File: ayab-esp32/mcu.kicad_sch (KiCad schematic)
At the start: 27 parts, among them J201 SPARE1, J202 SPARE0, Q201 AO3400A, SW201 USER, SW202 RESET, SW203 BOOTSEL, U201 ESP32-S3-MINI-1

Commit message: Correct footprint and regenerate documentation
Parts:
- D204: LCSC ID C2290 -> C22452; OEM Hubei KENTO Elec -> (none)
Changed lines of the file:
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@@
       (effects (font (size 1.27 1.27)) hide)
     )
-    (property "LCSC ID" "C2290" (at 247.65 41.91 0)
+    (property "LCSC ID" "C22452" (at 247.65 41.91 0)
       (effects (font (size 1.27 1.27)) hide)
     )
-    (property "OEM" "Hubei KENTO Elec" (at 247.65 41.91 0)
+    (property "OEM" "" (at 247.65 41.91 0)
       (effects (font (size 1.27 1.27)) hide)
     )

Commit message: add mouser parts list
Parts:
- BUZZER201: Mouser PN (none) -> 179-CMT-8504-99SMTTR
- C201, C202, C203, C204: Mouser PN (none) -> 187-CL10B104MB8NNNC
- C205: Mouser PN (none) -> 963-TMK212BBJ106KG-T
- D201: Mouser PN (none) -> 755-SML-H12Y8TT86C
- D202: Mouser PN (none) -> 749-SM0805PGC
- D203: Mouser PN (none) -> 749-SM0805RC
- D204: Mouser PN (none) -> 750-SS54B-HF
- J201, J202: Mouser PN (none) -> 855-M20-9750446
- R201, R205, R206, R207, R208, R211: Mouser PN (none) -> 791-RMC16K103FTP
- R202, R203, R204: Mouser PN (none) -> 603-AC0603FR-135K1L
- R212: Mouser PN (none) -> 71-CRCW06030000Z0EC
- U201: Mouser PN (none) -> 356-ESP32-S3-MINI1N8

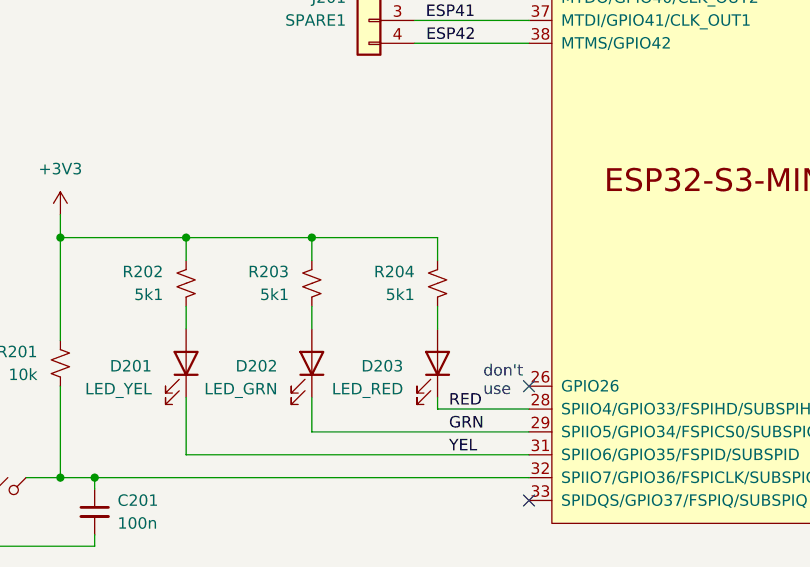
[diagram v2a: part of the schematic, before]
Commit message: address bringup issues
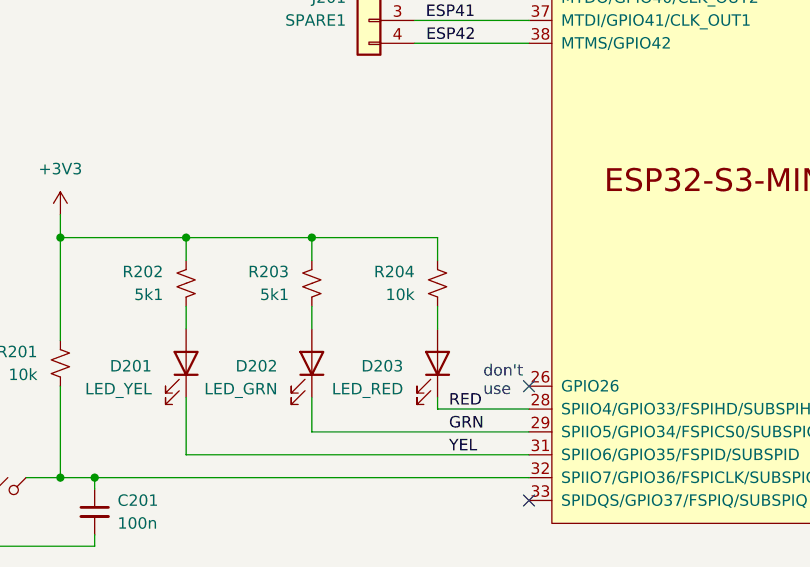
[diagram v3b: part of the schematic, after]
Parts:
- R204: value 5k1 -> 10k; LCSC ID C23186 -> C25804
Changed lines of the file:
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@@
 		(lib_id "ayab-lib:R_Small_US")
 		(at 83.82 104.14 0)
-		(mirror y)
 		(unit 1)
 		(exclude_from_sim no)
@@
 		(on_board yes)
 		(dnp no)
-		(fields_autoplaced yes)
 		(property "Reference" "R204"
-			(at 81.28 102.87 0)
+			(at 81.28 102.8699 0)
 			(effects
 				(font
 					(size 1.27 1.27)
 				)
-				(justify left)
+				(justify right)
 			)
 		)
-		(property "Value" "5k1"
-			(at 81.28 105.41 0)
+		(property "Value" "10k"
+			(at 81.28 105.4099 0)
 			(effects
 				(font
 					(size 1.27 1.27)
 				)
-				(justify left)
+				(justify right)
 			)
 		)
@@
 			)
 		)
-		(property "LCSC ID" "C23186"
+		(property "LCSC ID" "C25804"
 			(at 83.82 104.14 0)
 			(effects

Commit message: clean ERC DRC, fix library paths
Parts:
- BUZZER201: footprint easyeda2kicad:BUZ-SMD_4P-L8.5-W8.5-P8.50-BR -> Library:BUZ-SMD_4P-L8.5-W8.5-P8.50-BR
- SW201, SW202, SW203: footprint easyeda2kicad:KEY-TH_4P-L7.5-W11.5-P4.5 -> Library:KEY-TH_4P-L7.5-W11.5-P4.5
- U201: footprint Espressif:ESP32-S3-MINI-1 -> Library:ESP32-S3-MINI-1
